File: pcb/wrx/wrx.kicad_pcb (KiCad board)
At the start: 6 copper layers, 158 parts, among them J1 TB_2, J3 SMA, J4 DNL U.FL, M1 FPGA FIDUCIAL, M2 FPGA FIDUCIAL, M3 GLOBAL FIDUCIAL, U1 Artix-7 A35, U101 SE4150L, U104 LP5907 3.3V 250mA, U301 EEPROM 32Kx8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

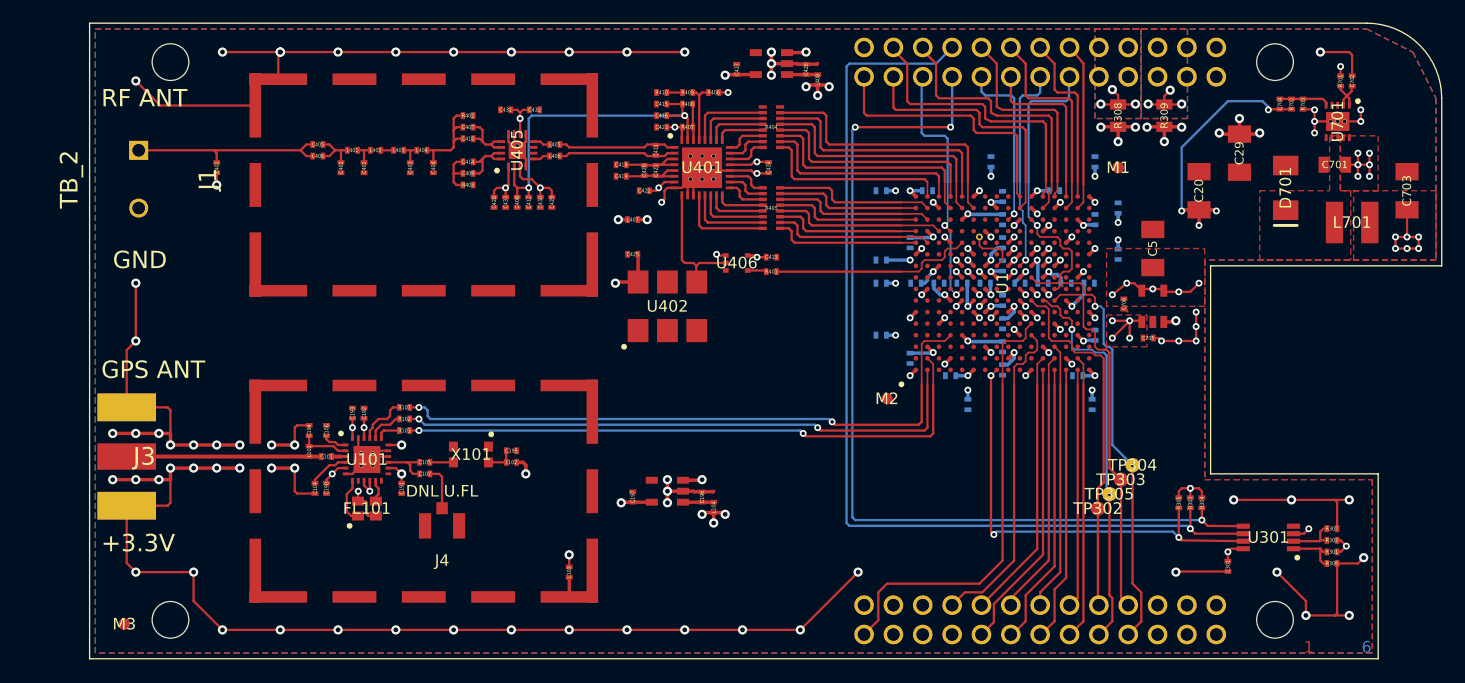
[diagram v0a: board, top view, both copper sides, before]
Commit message: big update to, and reorg of, PCB design files
The active antenna PCB has been split-out from the Beagle cape KiCAD
files. This was done so separate BOMs could be more easily created.
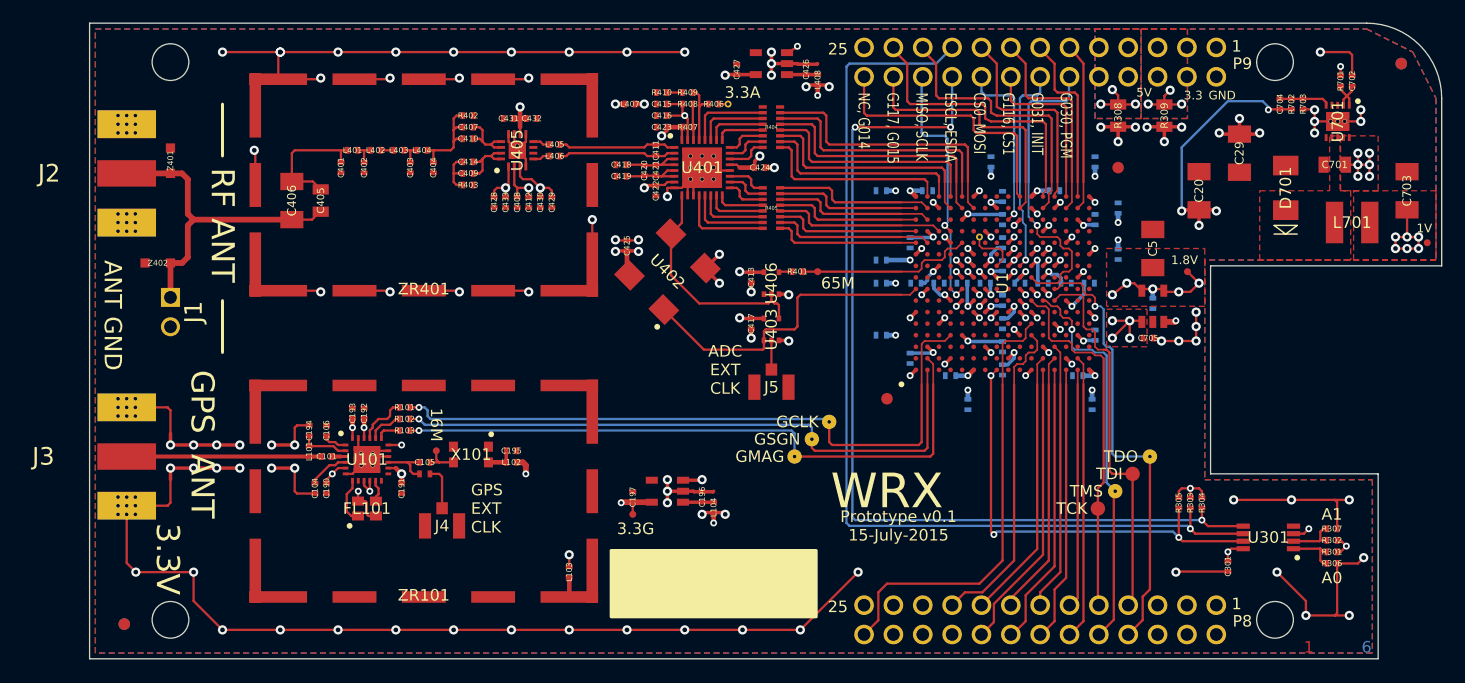
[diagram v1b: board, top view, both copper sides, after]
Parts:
- added C417: 10n, wrx-SM0402, F.Cu at (133.2, 98.5)
- added FID4: GLOBAL FIDUCIAL, wrx-FIDUCIAL, F.Cu at (189.5, 76.0)
- added FID5: GLOBAL FIDUCIAL, wrx-FIDUCIAL, B.Cu at (79.0, 124.5)
- added FID6: GLOBAL FIDUCIAL, wrx-FIDUCIAL, B.Cu at (189.5, 76.0)
- added J2: DNL BNC, wrx-BNC_SMA_EM, F.Cu at (76.0, 85.5)
- added J5: DNL U.FL, wrx-U.FL, F.Cu at (135.0, 104.0)
- added TP101: TEST_POINT, wrx-TP_600, F.Cu at (106.0, 109.5)
- added TP102: TEST_POINT, wrx-TP_VIA_1250, F.Cu at (140.0, 107.0)
- added TP103: TEST_POINT, wrx-TP_VIA_1250, F.Cu at (138.5, 108.5)
- added TP104: TEST_POINT, wrx-TP_VIA_1250, F.Cu at (137.0, 110.0)
- added TP105: TEST_POINT, wrx-TP_600, F.Cu at (123.0, 115.0)
- added TP401: TEST_POINT, wrx-TP_600, F.Cu at (139.0, 94.0)
- added TP402: TEST_POINT, wrx-TP_VIA_600, F.Cu at (131.2, 79.5)
- added TP701: TEST_POINT, wrx-TP_600, F.Cu at (191.8, 91.5)
- added TP702: TEST_POINT, wrx-TP_600, F.Cu at (171.0, 94.0)
- added U403: NC7SZ125, wrx-SC70_5, F.Cu at (135.0, 99.0)
- added Z402: TVS 3.3V, wrx-SOD323, F.Cu at (81.9, 93.2)
- C107: value 10n -> DNL 10n
- C401, C404: value 56p -> 56p/100
- C402, C403: value 160p -> 160p/50
- C405: value 1n -> 1n/100; footprint wrx-SM0402 -> wrx-SM0805
- C406: value 470n -> 470n/100; footprint wrx-SM0402 -> wrx-SM1206
- C706: moved to B.Cu
- J1: footprint wrx-TERM_BLOCK_2 -> wrx-TB_2P_2_54MM
- U402: value 65.360 MHz -> 66.6666 MHz; footprint wrx-VCXO -> wrx-XO
- U406: value NC7SZ126 -> NC7SZ125
- Z401: value TVS 40V -> TVS 3.3V; footprint wrx-SM0402 -> wrx-SOD323
- moved ZR102 83.1 mm to (104.9, 113.0)
- moved ZR402 60.5 mm to (104.9, 86.5)
- moved ZR101 17.9 mm to (104.9, 113.0)
- moved ZR401 17.9 mm to (104.9, 86.5)
- moved J1 11.8 mm to (83.0, 97.5)
- moved L407 10.0 mm to (122.8, 79.5)
- moved C405 4.86 mm to (96.0, 87.8), turned to 90 degrees
- moved C406 4.46 mm to (93.5, 87.8), turned to 90 degrees
- moved Z401 4.04 mm to (83.0, 84.4), turned to 270 degrees
- moved U406 3.47 mm to (135.0, 95.0), turned to 90 degrees
- moved U402 3.00 mm to (126.0, 94.0), turned to 135 degrees
- moved C706 2.50 mm to (168.0, 96.8)
- moved C413 2.47 mm to (133.2, 94.5), turned to 270 degrees
- moved R401 2.25 mm to (137.2, 94.0)
- moved TP304 1.68 mm to (167.8, 110.0)
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- renumbered M1 to FID1, M2 to FID2, M3 to FID3
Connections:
- U1 pad A8: (no net) -> AEXT
- U401 pad 9: /ADC/VCXO -> /ADC/AXO
- U402 pad 1: GND -> AEXT
- U402 pad 2: (no net) -> GND
- U402 pad 3: GND -> /ADC/AXO
- U402 pad 4: /ADC/VCXO -> 3.3A
- U406 pad 1: 3.3A -> GND
- U406 pad 2: /ADC/VCXO -> /ADC/AXO
- X101 pad 1: (no net) -> GND
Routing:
- net AEXT: track 0.00 -> 27.8 mm
- net /ADC/AXO: track 0.00 -> 19.6 mm
- net /ADC/VCXO: track 11.1 -> 0.00 mm
- net /ADC/ANT+: track 17.7 -> 28.6 mm
- net /ADC/LP1: track 4.61 -> 11.2 mm
- net GND: track 321.0 -> 325.8 mm, vias 108 -> 116
- net GMAG: track 52.3 -> 56.0 mm, vias 2 -> 1
- net GSGN: track 50.3 -> 53.8 mm, vias 2 -> 1
- net GCLK: track 54.9 -> 58.4 mm, vias 2 -> 1
- net 3.3A: track 19.6 -> 22.4 mm
- net /ADC/ECLK: track 0.00 -> 2.52 mm
- net /BeagleBone/TDO: track 36.2 -> 38.6 mm
- net ACLK: track 17.7 -> 15.4 mm
- net 1.8: track 17.6 -> 19.8 mm
- net /BeagleBone/TDI: track 31.8 -> 33.1 mm
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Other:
- board outline added: 117 x 55 mm
- board text added: "1.8V"
- board text added: "16M"
- board text added: "1V"
- board text added: "25"
- board text added: "3.3"
- board text added: "3.3A"
- board text added: "3.3G"
- board text added: "3.3V"
- board text added: "5V"
- board text added: "65M"
- board text added: "A0"
- board text added: "A1"
- board text added: "ADC EXT CLK"
- board text added: "ANT GND"
- board text added: "CS0, MOSI"
- board text added: "DO NOT LOAD RED COMPONENTS"
- board text added: "ESCL, ESDA"
- board text added: "G030, PGM"
- board text added: "G031, INIT"
- board text added: "G116, CS1"
- board text added: "G117, G015"
- board text added: "GCLK"
- board text added: "GMAG"
- board text added: "GPS EXT CLK"
- board text added: "GSGN"
- board text added: "MISO, SCLK"
- board text added: "NC, G014"
- board text added: "P8"
- board text added: "P9"
- board text added: "PROTOTYPE ONLY NOT FOR QUANTITY PRODUCTION"
- board text added: "Prototype v0.1 15-July-2015"
- board text added: "TCK"
- board text added: "TDI"
- board text added: "TDO"
- board text added: "TMS"
- board text added: "WRX"
- board text added: "WRX prototype v0.1 15-July-2015"
- board text removed: "+3.3V"
